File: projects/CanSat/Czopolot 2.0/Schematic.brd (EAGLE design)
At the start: 36.2 x 25.5 mm, 85 parts

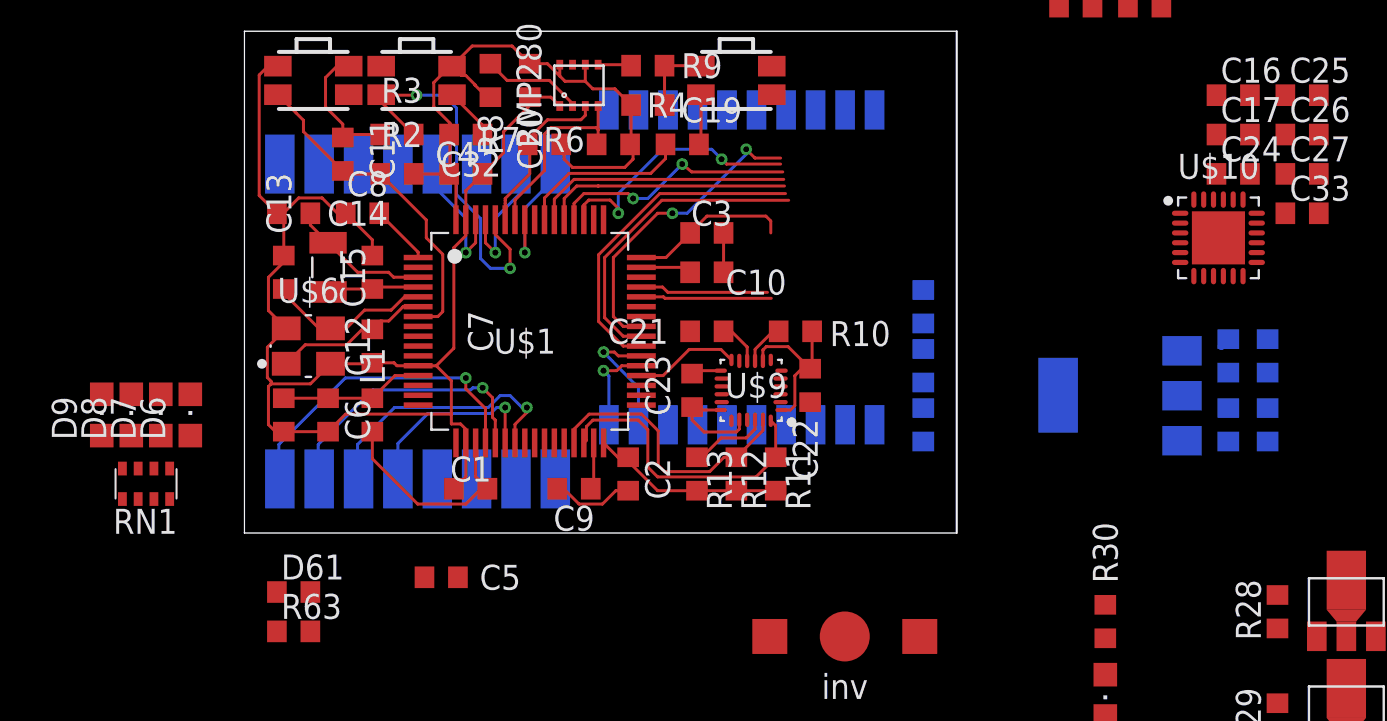
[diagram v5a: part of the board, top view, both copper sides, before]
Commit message: Updated charging solution for czopolot 2.0
Schematic update
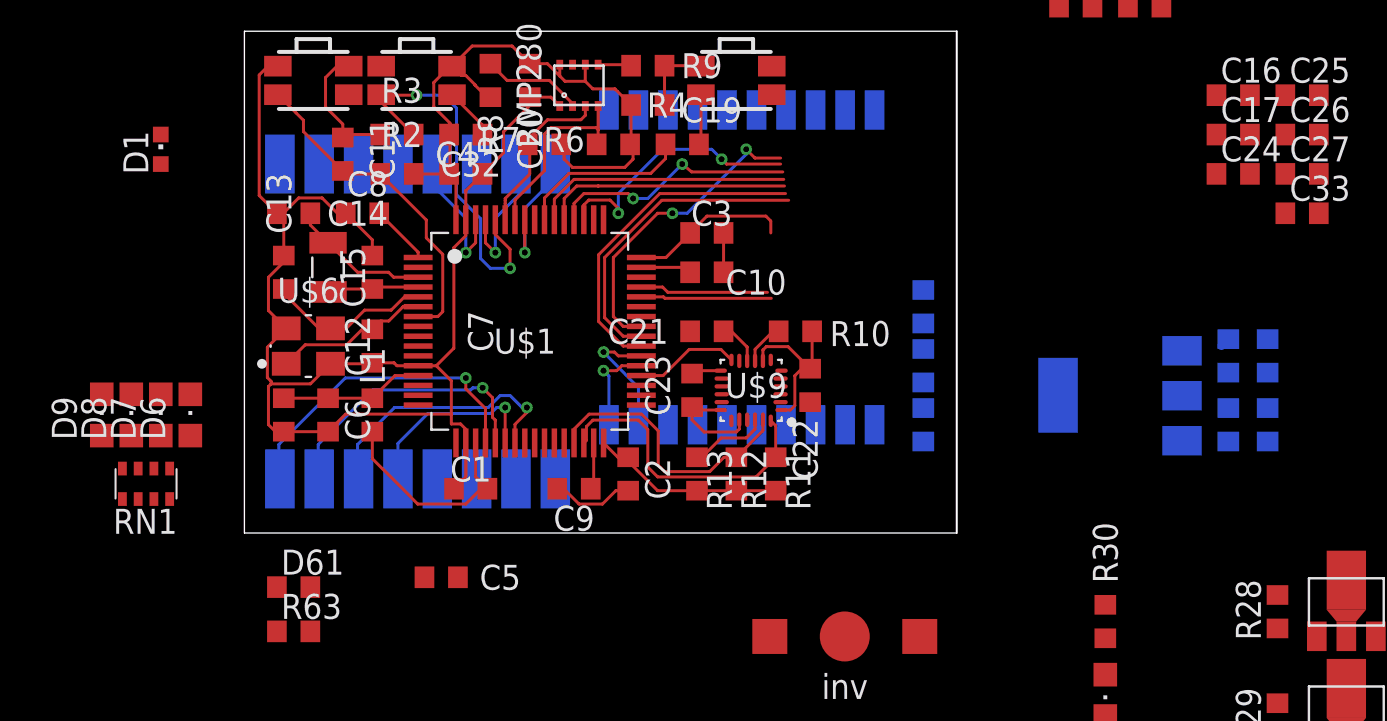
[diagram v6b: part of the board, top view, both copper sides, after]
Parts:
- removed U$10: BQ24270, SobieskiSat2:QFN50P400X400X100-25T270N
- added D1: (no value), Unified:CHIPLED_0603
- moved D61 0.25 mm to (2.50, -2.75)
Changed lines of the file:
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@@
 <attribute name="VALUE" x="3.25" y="7.2991" size="1.27" layer="27" align="top-center"/>
 </element>
-<element name="D61" library="Unified" package="R0603" package3d_urn="urn:adsk.eagle:package:23555/3" value="DIODE" x="2.5" y="-3" smashed="yes">
-<attribute name="NAME" x="1.865" y="-2.365" size="1.27" layer="25"/>
-<attribute name="VALUE" x="1.865" y="-4.905" size="1.27" layer="27"/>
+<element name="D61" library="Unified" package="R0603" package3d_urn="urn:adsk.eagle:package:23555/3" value="DIODE" x="2.5" y="-2.75" smashed="yes">
+<attribute name="NAME" x="1.865" y="-2.115" size="1.27" layer="25"/>
+<attribute name="VALUE" x="1.865" y="-4.655" size="1.27" layer="27"/>
 </element>
 <element name="R63" library="Unified" package="R0603" package3d_urn="urn:adsk.eagle:package:23555/3" value="10k" x="2.5" y="-5" smashed="yes">
@@
 </element>
 <element name="U$7" library="SobieskiSat2" package="USB-C" value="USB-C" x="53.5" y="40" smashed="yes"/>
-<element name="U$10" library="SobieskiSat2" package="QFN50P400X400X100-25T270N" package3d_urn="urn:adsk.eagle:package:15841520/1" value="BQ24270" x="49.5" y="15" smashed="yes">
-<attribute name="NAME" x="49.5" y="17.9996" size="1.27" layer="25" align="bottom-center"/>
-<attribute name="VALUE" x="49.5" y="12.0004" size="1.27" layer="27" align="top-center"/>
-</element>
 <element name="C16" library="Unified" package="C0603" package3d_urn="urn:adsk.eagle:package:23616/2" value="" x="50.25" y="22.25" smashed="yes">
 <attribute name="NAME" x="49.615" y="22.885" size="1.27" layer="25"/>
@@
 <attribute name="VALUE" x="53.115" y="14.345" size="1.27" layer="27"/>
 </element>
+<element name="D1" library="Unified" package="CHIPLED_0603" package3d_urn="urn:adsk.eagle:package:15822/2" value="" x="-4.25" y="19.5" smashed="yes">
+<attribute name="NAME" x="-4.885" y="18.23" size="1.27" layer="25" rot="R90"/>
+<attribute name="VALUE" x="-2.345" y="18.23" size="1.27" layer="27" rot="R90"/>
+</element>
 </elements>

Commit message: Work work..
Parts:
- removed C16, C17, C24, C25, C26, C27, C33: (no value), Unified:C0603
- added C34: 33n, Unified:C0603
- added C35: 22n, Unified:C0603
- added C36: (no value), Unified:C0603
- added C37: 1u, Unified:C0603
- added D2: LED0805, Unified:CHIPLED_0805
- added L2: 1uH, Unified:R0603
- added R14: pull down?, Unified:R0603
- added R15: 125R, Unified:R0603
- added R16, R17: NTC/5k, Unified:R0603
- added R5: (no value), Unified:R0603
- added U$10: BQ24253, SobieskiSat2:QFN50P400X400X100-25T270N
- moved R24 35.8 mm to (28.0, 12.2), turned to 0 degrees
- moved R23 33.0 mm to (28.0, 14.2), turned to 0 degrees
- moved U$11 8.53 mm to (53.0, 7.75), flipped to the top
- moved C28 6.54 mm to (45.5, 9.75), flipped to the top
- moved C31 6.54 mm to (45.5, 6.25), flipped to the top
- moved C29 2.61 mm to (47.5, 9.75), flipped to the top
- moved C30 2.61 mm to (47.5, 6.25), flipped to the top
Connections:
- new net BAT: U$10.11, U$10.12
- new net N$18: R15.2, U$10.10
- new net N$20: D2.C, U$10.7
- new net N$21: C34.1, L2.2, U$10.17, U$10.18
- new net N$22: C35.1, L2.1, U$10.13, U$10.14
- new net N$24: C36.1, U$10.20
- new net N$26: R16.1, R17.2, U$10.9
- new net N$27: R14.2, U$10.1
- new net N$28: D2.A, R5.1
- new net N$6: C34.2, U$10.21
- net GND: now also C35.2, C36.2, C37.1, R14.1, R15.1, R17.1, U$10.15, U$10.16, U$10.22, U$10.23, U$10.25, U$10.4
- net USB_D+: now also U$10.2
- net USB_D-: now also U$10.3
- net USB_VBUS: now also U$10.19
- net VCC: now also R5.2
- net VIN: now also C37.2, R16.2, U$10.24
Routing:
- net USB_D+: track 0.00 -> 1.81 mm
- net USB_D-: track 0.00 -> 1.70 mm
- net N$35: track 6.52 -> 7.89 mm
- net VCC: track 74.0 -> 73.1 mm

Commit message: change in ppm
Damian co ty tam zmieniasz LDO na VIN???
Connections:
- removed net N$22: C35.1, L2.1, U$10.13, U$10.14
- new net LDO: C37.2, R16.2, U$10.24
- net VIN: now also C35.1, L2.1, U$10.13, U$10.14; no longer C37.2, R16.2, U$10.24
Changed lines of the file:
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@@
 <contactref element="U$13" pad="P$2"/>
 <contactref element="D5" pad="2"/>
-<contactref element="R16" pad="2"/>
-<contactref element="U$10" pad="24"/>
-<contactref element="C37" pad="2"/>
-<wire x1="56.15" y1="17" x2="57.5" y2="22.6946" width="0" layer="19" extent="1-1"/>
-<wire x1="54.35" y1="15" x2="56.15" y2="17" width="0" layer="19" extent="1-1"/>
-<wire x1="49.9" y1="10.25" x2="54.35" y2="15" width="0" layer="19" extent="1-1"/>
+<contactref element="U$10" pad="13"/>
+<contactref element="U$10" pad="14"/>
+<contactref element="C35" pad="1"/>
+<contactref element="L2" pad="1"/>
+<wire x1="64.25" y1="17.4" x2="67" y2="20.15" width="0" layer="19" extent="1-1"/>
+<wire x1="60.6946" y1="19.5" x2="64.25" y2="17.4" width="0" layer="19" extent="1-1"/>
+<wire x1="60.6946" y1="20" x2="60.6946" y2="19.5" width="0" layer="19" extent="1-1"/>
+<wire x1="49.9" y1="10.25" x2="60.6946" y2="19.5" width="0" layer="19" extent="1-1"/>
 <wire x1="47.85" y1="10.25" x2="49.8504" y2="10.0106" width="0" layer="19" extent="1-1"/>
 <wire x1="45.5" y1="10.6" x2="47.5" y2="10.6" width="0" layer="19" extent="1-1"/>
@@
 <wire x1="59" y1="22.6946" x2="61.4" y2="25.5" width="0" layer="19" extent="1-1"/>
 </signal>
-<signal name="N$22">
-<contactref element="U$10" pad="13"/>
-<contactref element="U$10" pad="14"/>
-<contactref element="C35" pad="1"/>
-<contactref element="L2" pad="1"/>
-<wire x1="64.25" y1="17.4" x2="67" y2="20.15" width="0" layer="19" extent="1-1"/>
-<wire x1="60.6946" y1="19.5" x2="64.25" y2="17.4" width="0" layer="19" extent="1-1"/>
-<wire x1="60.6946" y1="20" x2="60.6946" y2="19.5" width="0" layer="19" extent="1-1"/>
-</signal>
 <signal name="N$24">
 <contactref element="U$10" pad="20"/>
@@
 <wire x1="46" y1="-5.55" x2="46" y2="-7.4" width="0" layer="19" extent="1-1"/>
 </signal>
+<signal name="LDO">
+<contactref element="R16" pad="2"/>
+<contactref element="U$10" pad="24"/>
+<contactref element="C37" pad="2"/>
+<wire x1="56.15" y1="17" x2="57.5" y2="22.6946" width="0" layer="19" extent="1-1"/>
+<wire x1="54.35" y1="15" x2="56.15" y2="17" width="0" layer="19" extent="1-1"/>
+</signal>
 </signals>
